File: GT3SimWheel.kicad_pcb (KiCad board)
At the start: 2 copper layers, 132 x 87 mm, 31 parts, among them SW1 SW_Push, SW10 SW_Push, SW11 RotaryEncoder_Switch, SW12 RotaryEncoder_Switch, SW13 SW_SPDT, SW14 SW_SPDT, SW2 SW_Push, SW3 SW_Push, SW4 SW_Push, SW5 SW_Push, SW6 SW_Push, SW7 SW_Push, SW8 SW_Push, SW9 SW_Push, U1 ProMicroC

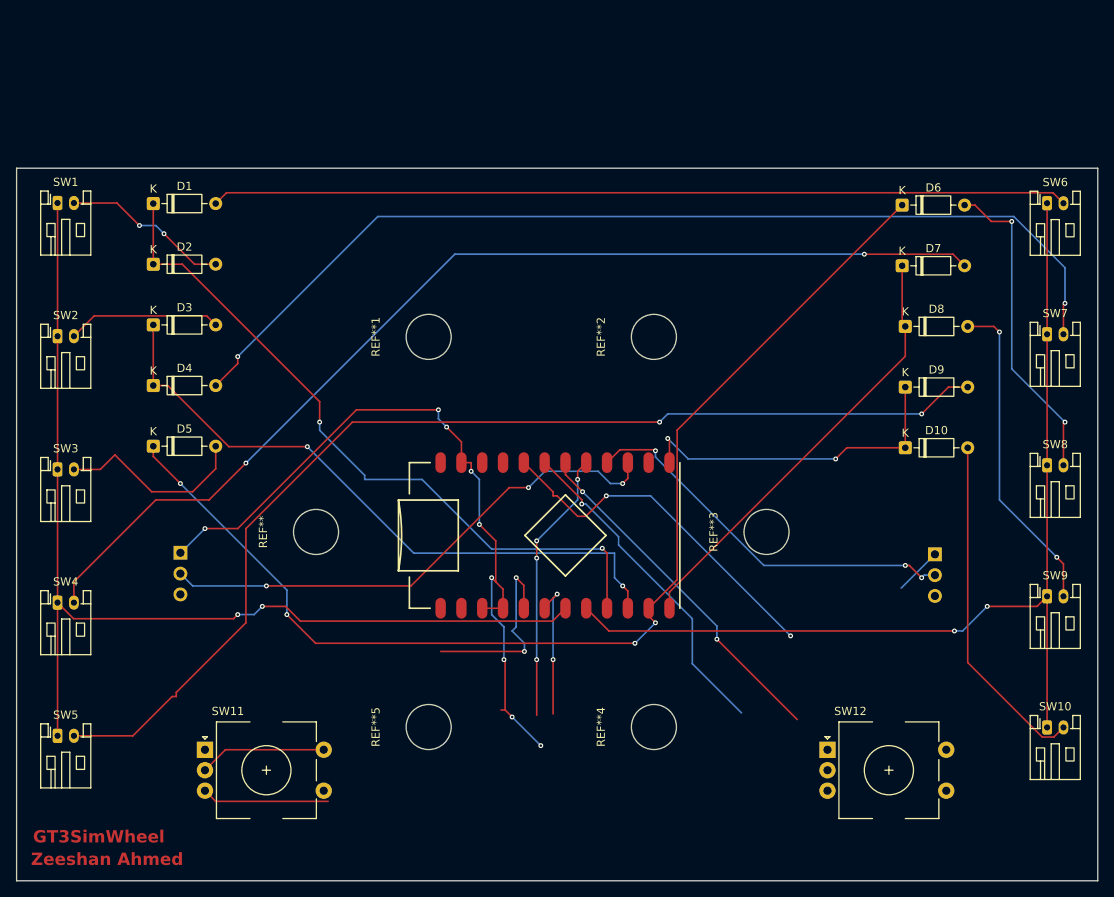
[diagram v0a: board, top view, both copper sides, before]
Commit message: Revert "v1 of mounting holes and traces"
This reverts commit 358c9c3b2d1fba7a0f09c887d354e31a74c0dc18.
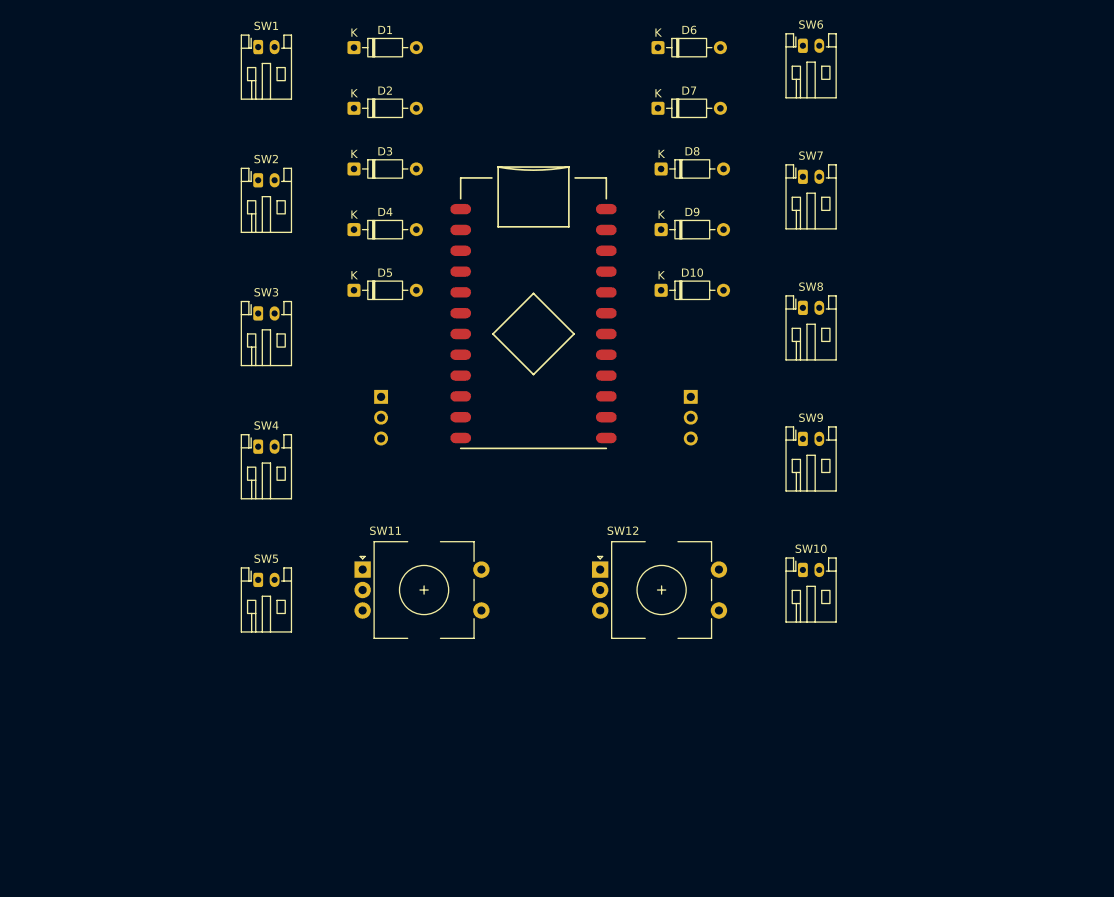
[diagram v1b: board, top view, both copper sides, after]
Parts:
- removed REF**, REF**1, REF**2, REF**3, REF**4, REF**5: MountingHole_5.5mm, MountingHole:MountingHole_5.5mm
- moved D6 35.5 mm to (178.8, 26.8)
- moved SW6 35.5 mm to (196.5, 26.6)
- moved SW7 35.5 mm to (196.5, 42.5)
- moved D10 35.5 mm to (179.2, 56.4)
- moved D7 35.5 mm to (178.8, 34.2)
- moved D8 35.5 mm to (179.2, 41.6)
- moved D9 35.5 mm to (179.2, 49.0)
- moved SW10 35.5 mm to (196.5, 90.5)
- moved SW14 35.5 mm to (182.8, 69.4)
- moved SW8 35.5 mm to (196.5, 58.5)
- moved SW9 35.5 mm to (196.5, 74.5)
- moved SW12 35.4 mm to (171.8, 90.5)
- moved D1 31.0 mm to (141.7, 26.8)
- moved D3 31.0 mm to (141.7, 41.6)
- moved SW1 31.0 mm to (130.0, 26.7)
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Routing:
- net /col3: track 139.0 -> 0.00 mm, vias 4 -> 0
- net Net-(D9-A): track 133.8 -> 0.00 mm, vias 2 -> 0
- net /row1: track 129.9 -> 0.00 mm, vias 2 -> 0
- net Net-(D7-A): track 128.4 -> 0.00 mm, vias 2 -> 0
- net Net-(D4-A): track 123.5 -> 0.00 mm, vias 2 -> 0
- net /row2: track 123.2 -> 0.00 mm, vias 2 -> 0
- net GND: track 115.0 -> 0.00 mm, vias 9 -> 0
- net Net-(D1-A): track 104.6 -> 0.00 mm
- net /col1: track 86.6 -> 0.00 mm, vias 2 -> 0
- net /col2: track 79.6 -> 0.00 mm, vias 2 -> 0
- net /SW13: track 63.9 -> 0.00 mm, vias 3 -> 0
- net /col4: track 53.9 -> 0.00 mm
- net /SW14: track 47.7 -> 0.00 mm, vias 3 -> 0
- net /ENC2SW: track 43.7 -> 0.00 mm, vias 2 -> 0
- net /ENC2A: track 43.1 -> 0.00 mm, vias 2 -> 0
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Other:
- board outline removed
- board text removed: "GT3SimWheel"
- board text removed: "Zeeshan Ahmed"

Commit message: v1 of mounting holes and traces
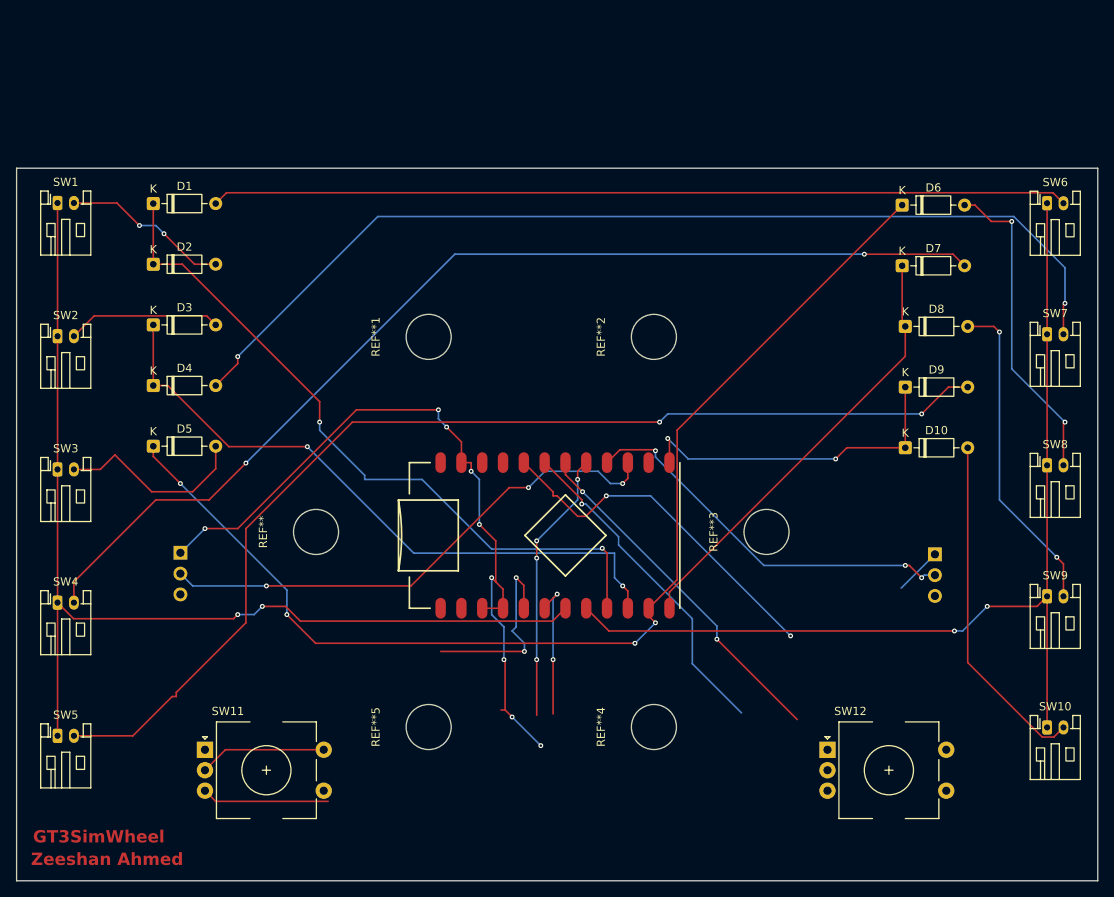
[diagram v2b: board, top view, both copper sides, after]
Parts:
- added REF**: MountingHole_5.5mm, MountingHole:MountingHole_5.5mm, F.Cu at (137.1, 85.9)
- added REF**1: MountingHole_5.5mm, MountingHole:MountingHole_5.5mm, F.Cu at (150.8, 62.1)
- added REF**2: MountingHole_5.5mm, MountingHole:MountingHole_5.5mm, F.Cu at (178.3, 62.1)
- added REF**3: MountingHole_5.5mm, MountingHole:MountingHole_5.5mm, F.Cu at (192.1, 85.9)
- added REF**4: MountingHole_5.5mm, MountingHole:MountingHole_5.5mm, F.Cu at (178.3, 109.7)
- added REF**5: MountingHole_5.5mm, MountingHole:MountingHole_5.5mm, F.Cu at (150.8, 109.7)
- moved D6 35.5 mm to (208.6, 46.0)
- moved SW6 35.5 mm to (226.3, 45.8)
- moved SW7 35.5 mm to (226.3, 61.8)
- moved D10 35.5 mm to (209.0, 75.6)
- moved D7 35.5 mm to (208.6, 53.4)
- moved D8 35.5 mm to (209.0, 60.8)
- moved D9 35.5 mm to (209.0, 68.2)
- moved SW10 35.5 mm to (226.3, 109.8)
- moved SW14 35.5 mm to (212.6, 88.6)
- moved SW8 35.5 mm to (226.3, 77.8)
- moved SW9 35.5 mm to (226.3, 93.8)
- moved SW12 35.4 mm to (199.5, 112.5)
- moved D1 31.0 mm to (117.2, 45.8)
- moved D3 31.0 mm to (117.2, 60.6)
- moved SW1 31.0 mm to (105.5, 45.8)
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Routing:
- net /col3: track 0.00 -> 139.0 mm, vias 0 -> 4
- net Net-(D9-A): track 0.00 -> 133.8 mm, vias 0 -> 2
- net /row1: track 0.00 -> 129.9 mm, vias 0 -> 2
- net Net-(D7-A): track 0.00 -> 128.4 mm, vias 0 -> 2
- net Net-(D4-A): track 0.00 -> 123.5 mm, vias 0 -> 2
- net /row2: track 0.00 -> 123.2 mm, vias 0 -> 2
- net GND: track 0.00 -> 115.0 mm, vias 0 -> 9
- net Net-(D1-A): track 0.00 -> 104.6 mm
- net /col1: track 0.00 -> 86.6 mm, vias 0 -> 2
- net /col2: track 0.00 -> 79.6 mm, vias 0 -> 2
- net /SW13: track 0.00 -> 63.9 mm, vias 0 -> 3
- net /col4: track 0.00 -> 53.9 mm
- net /SW14: track 0.00 -> 47.7 mm, vias 0 -> 3
- net /ENC2SW: track 0.00 -> 43.7 mm, vias 0 -> 2
- net /ENC2A: track 0.00 -> 43.1 mm, vias 0 -> 2
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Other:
- board outline added: 132 x 87 mm
- board text added: "GT3SimWheel"
- board text added: "Zeeshan Ahmed"
